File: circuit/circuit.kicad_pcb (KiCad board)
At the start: 2 copper layers, 33 x 33 mm, 10 parts

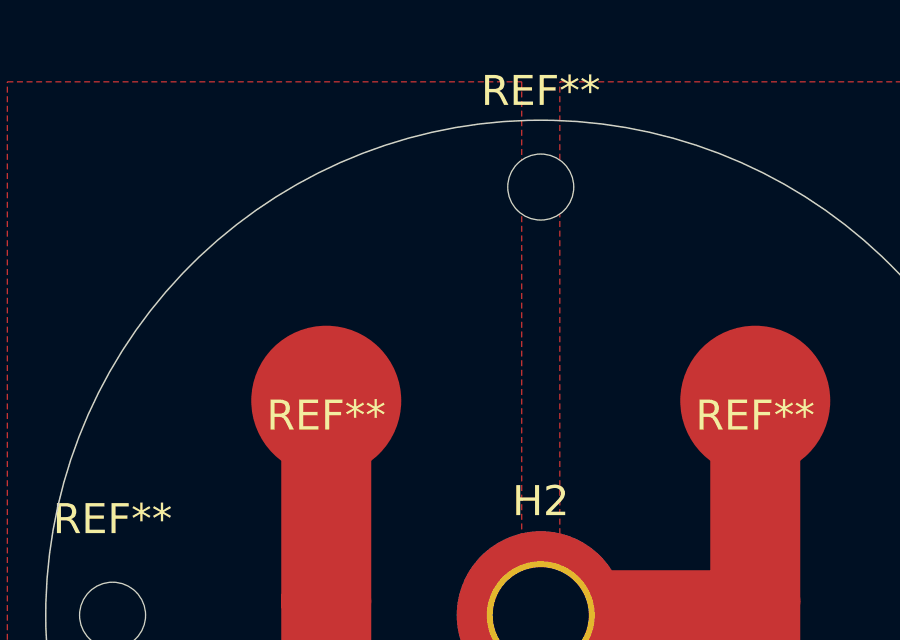
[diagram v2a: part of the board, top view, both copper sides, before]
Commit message: making provisions for 2 wires to go down the sides to increase amperage with the dupont connector option
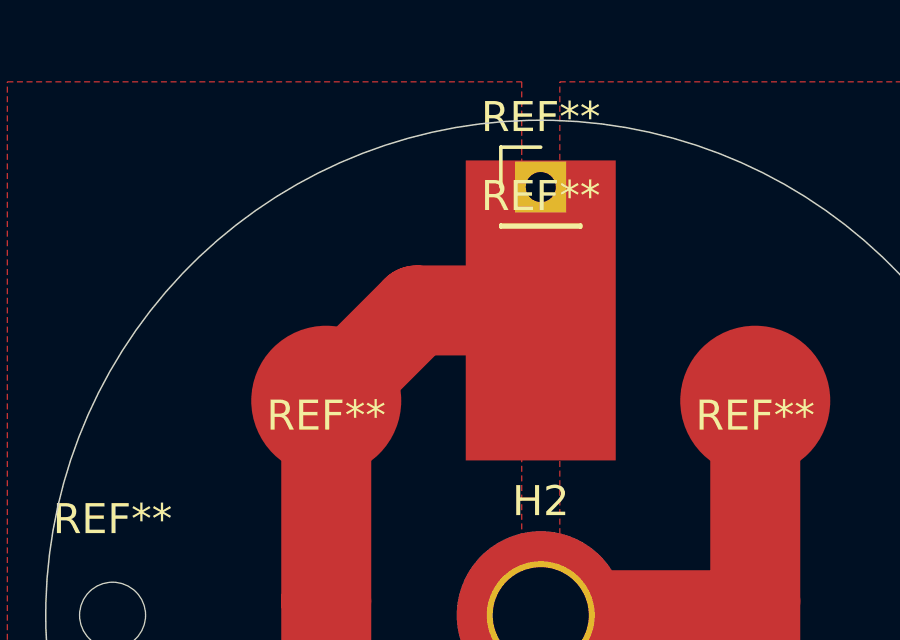
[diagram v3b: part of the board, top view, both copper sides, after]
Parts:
- removed the REF** at (177.8, 74.6)
- added REF**: SolderWirePad_1x01_SMD_5x10mm, Connector_Wire:SolderWirePad_1x01_SMD_5x10mm, F.Cu at (177.8, 78.7)
- added REF**: PinHeader_1x01_P2.54mm_Vertical, Connector_PinHeader_2.54mm:PinHeader_1x01_P2.54mm_Vertical, F.Cu at (177.8, 74.6)
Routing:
- net VSS: track 22.7 -> 31.1 mm
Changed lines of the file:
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@@
     (thickness 1.6)
     (drawings 5)
-    (tracks 8)
+    (tracks 10)
     (zones 0)
-    (modules 10)
+    (modules 11)
     (nets 3)
   )
@@
     (mod_text_size 1 1)
     (mod_text_width 0.15)
-    (pad_size 1.7 1.7)
-    (pad_drill 1)
+    (pad_size 5 10)
+    (pad_drill 0)
     (pad_to_mask_clearance 0)
     (aux_axis_origin 0 0)
@@
     (add_net VSS)
   )
+  (module Connector_Wire:SolderWirePad_1x01_SMD_5x10mm (layer F.Cu)
+    (at 177.8 78.74)
+    (descr "Wire Pad, Square, SMD Pad,  5mm x 10mm,")
+    (tags "MesurementPoint Square SMDPad 5mmx10mm ")
+    (fp_text reference REF** (at 0 -3.81) (layer F.SilkS)
+      (effects (font (size 1 1) (thickness 0.15)))
+    )
+    (fp_text value SolderWirePad_1x01_SMD_5x10mm (at 0 6.35) (layer F.Fab)
+      (effects (font (size 1 1) (thickness 0.15)))
+    )
+    (fp_text user %R (at 0 0) (layer F.Fab)
+      (effects (font (size 1 1) (thickness 0.15)))
+    )
+    (fp_line (start 2.75 -5.25) (end -2.75 -5.25) (layer F.CrtYd) (width 0.05))
+    (fp_line (start 2.75 5.25) (end 2.75 -5.25) (layer F.CrtYd) (width 0.05))
+    (fp_line (start -2.75 5.25) (end 2.75 5.25) (layer F.CrtYd) (width 0.05))
+    (fp_line (start -2.75 -5.25) (end -2.75 5.25) (layer F.CrtYd) (width 0.05))
+    (pad 1 smd rect (at 0 0) (size 5 10) (layers F.Cu F.Paste F.Mask)
+      (net 2 VSS))
+  )
   (module Connector_PinHeader_2.54mm:PinHeader_1x01_P2.54mm_Vertical (layer F.Cu)
-    (at 177.8 100.33)
+    (at 177.8 74.6276)
     (descr "Through hole straight pin header, 1x01, 2.54mm pitch, single row")
     (tags "Through hole pin header THT 1x01 2.54mm single row")
@@
     (fp_line (start 1.8 1.8) (end 1.8 -1.8) (layer F.CrtYd) (width 0.05))
     (fp_line (start 1.8 -1.8) (end -1.8 -1.8) (layer F.CrtYd) (width 0.05))
-    (pad 1 thru_hole rect (at 0 2.8424) (size 1.7 1.7) (drill 1) (layers *.Cu *.Mask)
+    (pad 1 thru_hole rect (at 0 0) (size 1.7 1.7) (drill 1) (layers *.Cu *.Mask)
       (net 2 VSS))
     (model ${KISYS3DMOD}/Connector_PinHeader_2.54mm.3dshapes/PinHeader_1x01_P2.54mm_Vertical.wrl
@@
     )
   )
+  (module Connector_PinHeader_2.54mm:PinHeader_1x01_P2.54mm_Vertical (layer F.Cu)
+    (at 177.8 100.33)
+    (descr "Through hole straight pin header, 1x01, 2.54mm pitch, single row")
+    (tags "Through hole pin header THT 1x01 2.54mm single row")
+    (fp_text reference REF** (at 0 -2.33) (layer F.SilkS)
+      (effects (font (size 1 1) (thickness 0.15)))
+    )
+    (fp_text value PinHeader_1x01_P2.54mm_Vertical (at 0 2.33) (layer F.Fab)
+      (effects (font (size 1 1) (thickness 0.15)))
+    )
+    (fp_line (start 1.8 -1.8) (end -1.8 -1.8) (layer F.CrtYd) (width 0.05))
+    (fp_line (start 1.8 1.8) (end 1.8 -1.8) (layer F.CrtYd) (width 0.05))
+    (fp_line (start -1.8 1.8) (end 1.8 1.8) (layer F.CrtYd) (width 0.05))
+    (fp_line (start -1.8 -1.8) (end -1.8 1.8) (layer F.CrtYd) (width 0.05))
+    (fp_line (start -1.33 -1.33) (end 0 -1.33) (layer F.SilkS) (width 0.12))
+    (fp_line (start -1.33 0) (end -1.33 -1.33) (layer F.SilkS) (width 0.12))
+    (fp_line (start -1.33 1.27) (end 1.33 1.27) (layer F.SilkS) (width 0.12))
+    (fp_line (start 1.33 1.27) (end 1.33 1.33) (layer F.SilkS) (width 0.12))
+    (fp_line (start -1.33 1.27) (end -1.33 1.33) (layer F.SilkS) (width 0.12))
+    (fp_line (start -1.33 1.33) (end 1.33 1.33) (layer F.SilkS) (width 0.12))
+    (fp_line (start -1.27 -0.635) (end -0.635 -1.27) (layer F.Fab) (width 0.1))
+    (fp_line (start -1.27 1.27) (end -1.27 -0.635) (layer F.Fab) (width 0.1))
+    (fp_line (start 1.27 1.27) (end -1.27 1.27) (layer F.Fab) (width 0.1))
+    (fp_line (start 1.27 -1.27) (end 1.27 1.27) (layer F.Fab) (width 0.1))
+    (fp_line (start -0.635 -1.27) (end 1.27 -1.27) (layer F.Fab) (width 0.1))
+    (fp_text user %R (at 0 0 90) (layer F.Fab)
+      (effects (font (size 1 1) (thickness 0.15)))
+    )
+    (pad 1 thru_hole rect (at 0 2.8424) (size 1.7 1.7) (drill 1) (layers *.Cu *.Mask)
+      (net 2 VSS))
+    (model ${KISYS3DMOD}/Connector_PinHeader_2.54mm.3dshapes/PinHeader_1x01_P2.54mm_Vertical.wrl
+      (at (xyz 0 0 0))
+      (scale (xyz 1 1 1))
+      (rotate (xyz 0 0 0))
+    )
+  )
   (module Pad_5mm (layer F.Cu)
     (at 184.95 96.05)
@@
     (pad 1 smd circle (at 0 0) (size 5 5) (layers F.Cu F.Paste F.Mask)
       (net 2 VSS))
-  )
-  (module MountingHole:MountingHole_2.2mm_M2 (layer F.Cu)
-    (at 177.8 74.6276)
-    (descr "Mounting Hole 2.2mm, no annular, M2")
-    (tags "mounting hole 2.2mm no annular m2")
-    (attr virtual)
-    (fp_text reference REF** (at 0 -3.2) (layer F.SilkS)
-      (effects (font (size 1 1) (thickness 0.15)))
-    )
-    (fp_text value MountingHole_2.2mm_M2 (at 0 3.2) (layer F.Fab)
-      (effects (font (size 1 1) (thickness 0.15)))
-    )
-    (fp_circle (center 0 0) (end 2.45 0) (layer F.CrtYd) (width 0.05))
-    (fp_circle (center 0 0) (end 2.2 0) (layer Cmts.User) (width 0.15))
-    (fp_text user %R (at 0.3 0) (layer F.Fab)
-      (effects (font (size 1 1) (thickness 0.15)))
-    )
-    (pad 1 np_thru_hole circle (at 0 0) (size 2.2 2.2) (drill 2.2) (layers *.Cu *.Mask))
   )
   (module Connector_Wire:SolderWirePad_1x01_SMD_5x10mm (layer F.Cu)
@@
       (effects (font (size 1 1) (thickness 0.15)))
     )
+    (fp_line (start 2.75 -5.25) (end -2.75 -5.25) (layer F.CrtYd) (width 0.05))
+    (fp_line (start 2.75 5.25) (end 2.75 -5.25) (layer F.CrtYd) (width 0.05))
+    (fp_line (start -2.75 5.25) (end 2.75 5.25) (layer F.CrtYd) (width 0.05))
     (fp_line (start -2.75 -5.25) (end -2.75 5.25) (layer F.CrtYd) (width 0.05))
-    (fp_line (start -2.75 5.25) (end 2.75 5.25) (layer F.CrtYd) (width 0.05))
-    (fp_line (start 2.75 5.25) (end 2.75 -5.25) (layer F.CrtYd) (width 0.05))
-    (fp_line (start 2.75 -5.25) (end -2.75 -5.25) (layer F.CrtYd) (width 0.05))
     (fp_text user %R (at 0 0) (layer F.Fab)
       (effects (font (size 1 1) (thickness 0.15)))
@@
       (effects (font (size 1 1) (thickness 0.15)))
     )
+    (fp_circle (center 0 0) (end 2.45 0) (layer F.CrtYd) (width 0.05))
     (fp_circle (center 0 0) (end 2.2 0) (layer Cmts.User) (width 0.15))
-    (fp_circle (center 0 0) (end 2.45 0) (layer F.CrtYd) (width 0.05))
     (fp_text user %R (at 2.8424 0) (layer F.Fab)
       (effects (font (size 1 1) (thickness 0.15)))
@@
       (effects (font (size 1 1) (thickness 0.15)))
     )
+    (fp_circle (center 0 0) (end 2.45 0) (layer F.CrtYd) (width 0.05))
     (fp_circle (center 0 0) (end 2.2 0) (layer Cmts.User) (width 0.15))
-    (fp_circle (center 0 0) (end 2.45 0) (layer F.CrtYd) (width 0.05))
     (fp_text user %R (at 0.3 0) (layer F.Fab)
       (effects (font (size 1 1) (thickness 0.15)))
@@
       (effects (font (size 1 1) (thickness 0.15)))
     )
+    (fp_circle (center 0 0) (end 3.05 0) (layer F.CrtYd) (width 0.05))
     (fp_circle (center 0 0) (end 2.8 0) (layer Cmts.User) (width 0.15))
-    (fp_circle (center 0 0) (end 3.05 0) (layer F.CrtYd) (width 0.05))
     (fp_text user %R (at 0.3 0) (layer F.Fab)
       (effects (font (size 1 1) (thickness 0.15)))
@@
   (segment (start 173.66 99.06) (end 170.65 96.05) (width 3) (layer F.Cu) (net 2))
   (segment (start 177.8 99.06) (end 173.66 99.06) (width 3) (layer F.Cu) (net 2))
+  (segment (start 173.66 78.74) (end 170.65 81.75) (width 3) (layer F.Cu) (net 2))
+  (segment (start 177.8 78.74) (end 173.66 78.74) (width 3) (layer F.Cu) (net 2))
   (zone (net 1) (net_name GND) (layer F.Cu) (hatch edge 0.508)
     (priority 1)
